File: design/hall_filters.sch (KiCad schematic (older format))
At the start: 11 parts

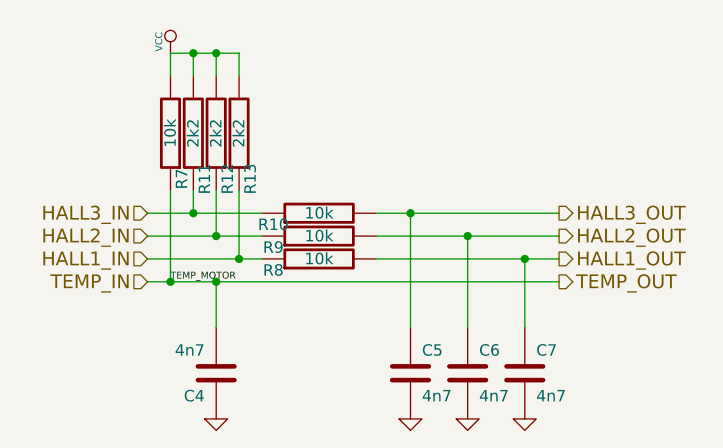
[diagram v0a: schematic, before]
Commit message: Implemented some improvements in schematic, but layout is completely new.
Changes in schematic:
- 3.3V or 5V CAN transceiver can be used
- DRV8301 can also be used and configured via SPI
- JTAG connector changed
- Fixed pinning of P1
- Some additional decoupling and/or filtering of analog signals
- Improved buck design according TI Webench recommendation
- Changed some component values
- maybe others...

Changes in layout:
- completely new layout
- placement of the big components is unchanged
- CAN connector rotated by 180°
- kept one layer free as a good GND plane
- many traces should be shorter and have lower impedance now
- improved buck layout

Other changes:
- updated gerber files
- updated PDFs (schematic and component placement)
- deleted all outdated files except libraries and datasheets
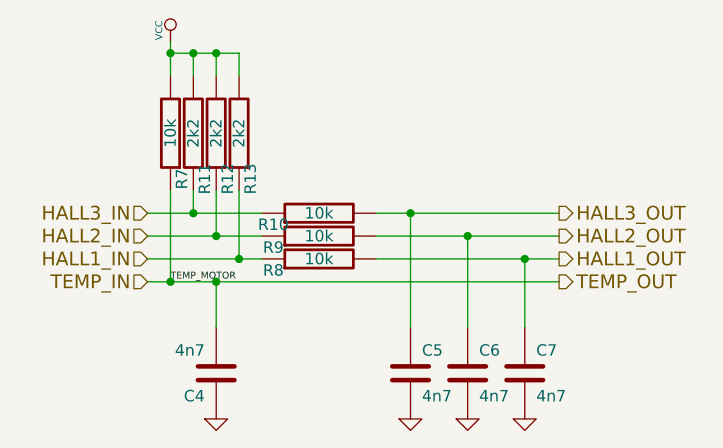
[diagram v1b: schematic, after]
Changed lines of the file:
@@
 EESchema Schematic File Version 2
-LIBS:BLDC_4-rescue
 LIBS:power
 LIBS:device
@@
 LIBS:contrib
 LIBS:valves
-LIBS:crf_1
 LIBS:BLDC_4-cache
 EELAYER 25 0
@@
 encoding utf-8
 Sheet 5 7
-Title "BLDC Driver 4.11"
-Date "21 aug 2015"
-Rev "4.11"
+Title "BLDC Driver 4.11p"
+Date "2016-01-06"
+Rev "A"
 Comp "Benjamin Vedder"
-Comment1 ""
+Comment1 "modified by pikim"
 Comment2 ""
 Comment3 ""
@@
 	1    0    0    -1
 $EndComp
-$Comp
-L VCC #PWR032
-U 1 1 53FBB5DA
-P 4900 2850
-F 0 "#PWR032" H 4900 2950 30  0001 C CNN
-F 1 "VCC" V 4850 2900 30  0000 C CNN
-F 2 "" H 4900 2850 60  0001 C CNN
-F 3 "" H 4900 2850 60  0001 C CNN
-	1    4900 2850
-	1    0    0    -1
-$EndComp
 Connection ~ 5950 3550
 Connection ~ 6200 3650
@@
 	5100 3850 5100 4050
 $Comp
-L GND-RESCUE-BLDC_4 #PWR033
+L GND-RESCUE-BLDC_4 #PWR032
 U 1 1 53FBB5F9
 P 6200 4450
-F 0 "#PWR033" H 6200 4450 30  0001 C CNN
+F 0 "#PWR032" H 6200 4450 30  0001 C CNN
 F 1 "GND" H 6200 4380 30  0001 C CNN
 F 2 "" H 6200 4450 60  0001 C CNN
@@
 $EndComp
 $Comp
-L GND-RESCUE-BLDC_4 #PWR034
+L GND-RESCUE-BLDC_4 #PWR033
 U 1 1 53FBB5FF
 P 6450 4450
-F 0 "#PWR034" H 6450 4450 30  0001 C CNN
+F 0 "#PWR033" H 6450 4450 30  0001 C CNN
 F 1 "GND" H 6450 4380 30  0001 C CNN
 F 2 "" H 6450 4450 60  0001 C CNN
@@
 Connection ~ 4900 3850
 Wire Wire Line
-	4900 2850 4900 2950
+	4900 2800 4900 2950
 Wire Wire Line
 	4900 2850 5200 2850
@@
 Text HLabel 6600 3850 2    60   Output ~ 0
 TEMP_OUT
+Connection ~ 4900 2850
+$Comp
+L VCC #PWR034
+U 1 1 53FBB5DA
+P 4900 2800
+F 0 "#PWR034" H 4900 2900 30  0001 C CNN
+F 1 "VCC" V 4850 2850 30  0000 C CNN
+F 2 "" H 4900 2800 60  0001 C CNN
+F 3 "" H 4900 2800 60  0001 C CNN
+	1    4900 2800
+	1    0    0    -1
+$EndComp
 $EndSCHEMATC
